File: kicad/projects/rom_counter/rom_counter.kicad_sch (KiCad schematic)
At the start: 42 parts, among them J1 peripheral_addr_bus_connector, J2 peripheral_aux_connector, J3 peripheral_membank_connector, J4 Conn_02x16_Odd_Even, J5 Conn_01x16_Socket, J6 Conn_01x02_Socket, J7 Conn_01x02_Pin, U1 28C256, U10 74HC161, U11 74HC245, U12 74HC245, U2 28C256, U3 74HC30, U4 74HC30, U5 74HC32, U6 74HC00, U7 74HC161, U8 74HC161, U9 74HC161

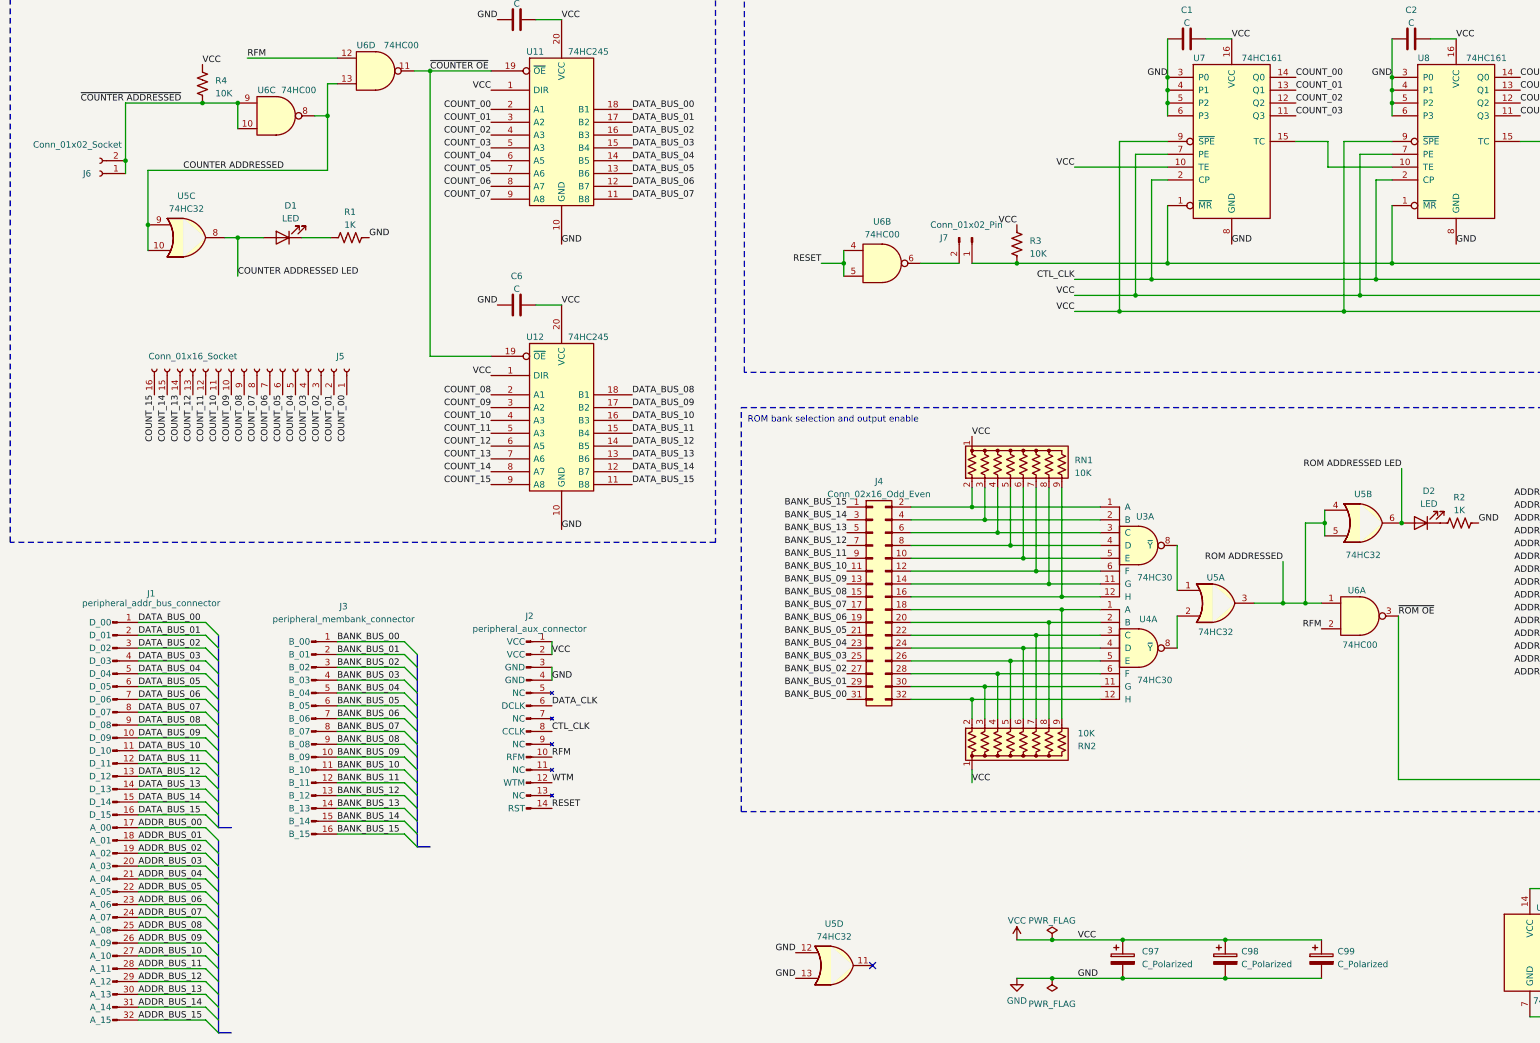
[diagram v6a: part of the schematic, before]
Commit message: PCB for ROM counter done - still needs tech checks
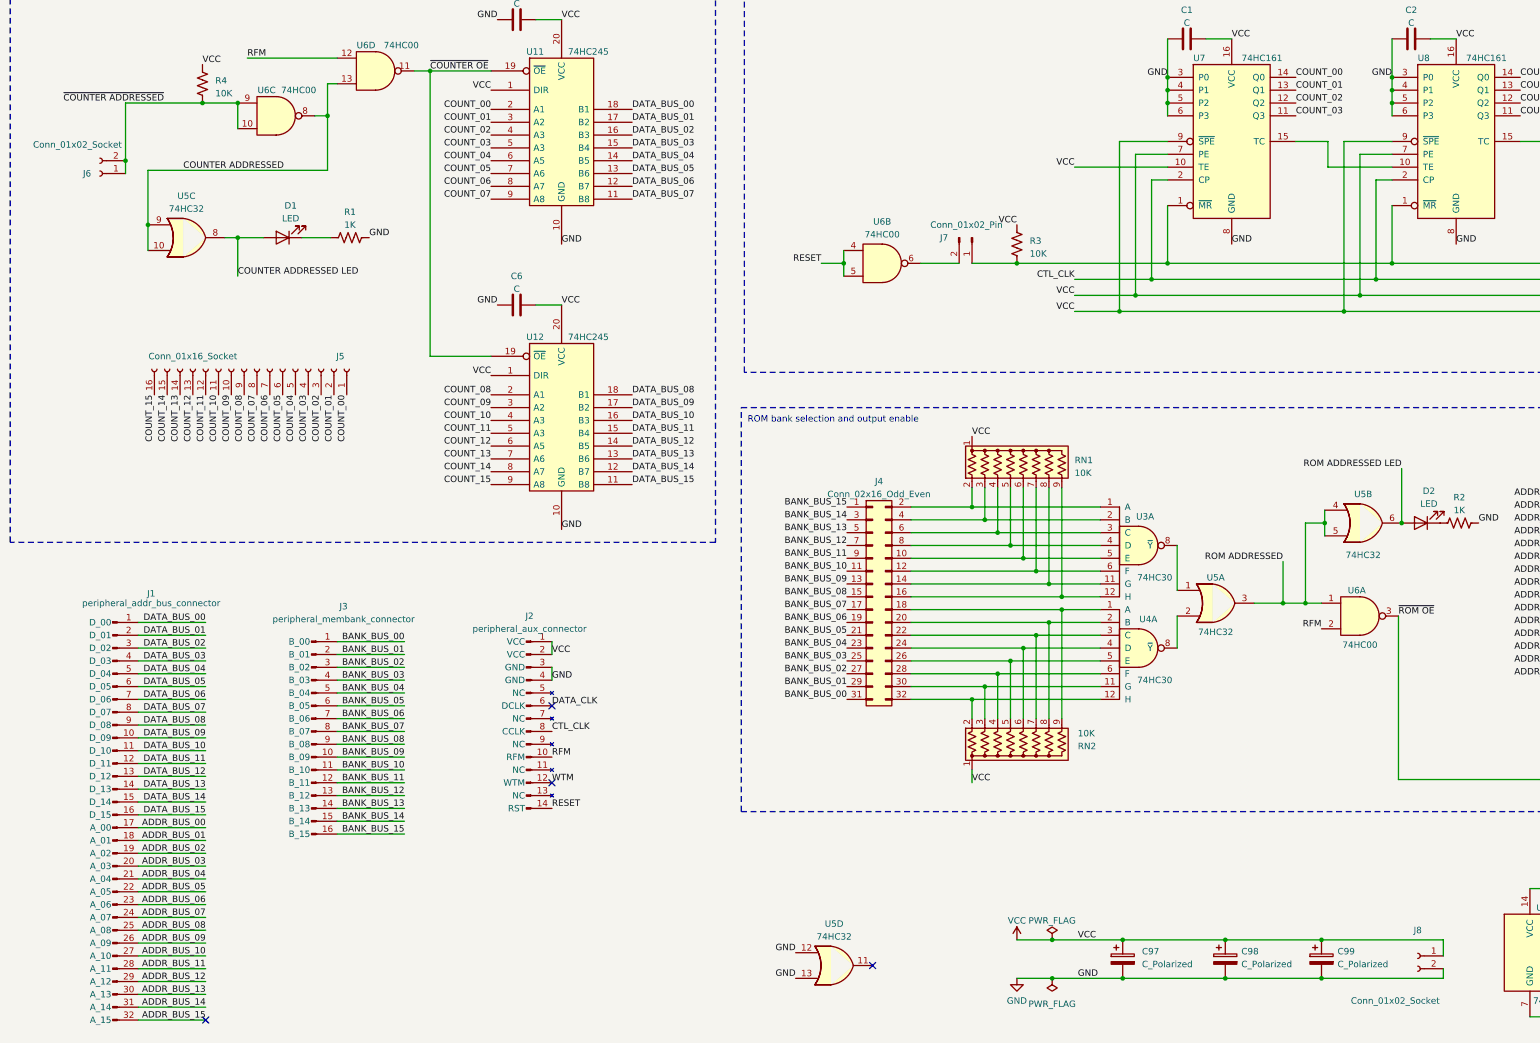
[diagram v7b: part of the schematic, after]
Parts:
- added J8: Conn_01x02_Socket, Connector_PinSocket_2.54mm:PinSocket_1x02_P2.54mm_Horizontal, symbol Connector:Conn_01x02_Socket
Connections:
- net GND: now also J8.2 (Pin_2)
- net VCC: now also J8.1 (Pin_1)
- net ~{COUNTER ADDRESSED}: now also J6.1 (Pin_1), J6.2 (Pin_2), R4.1, U6.10, U6.9
- no-connect marks 2 -> 5

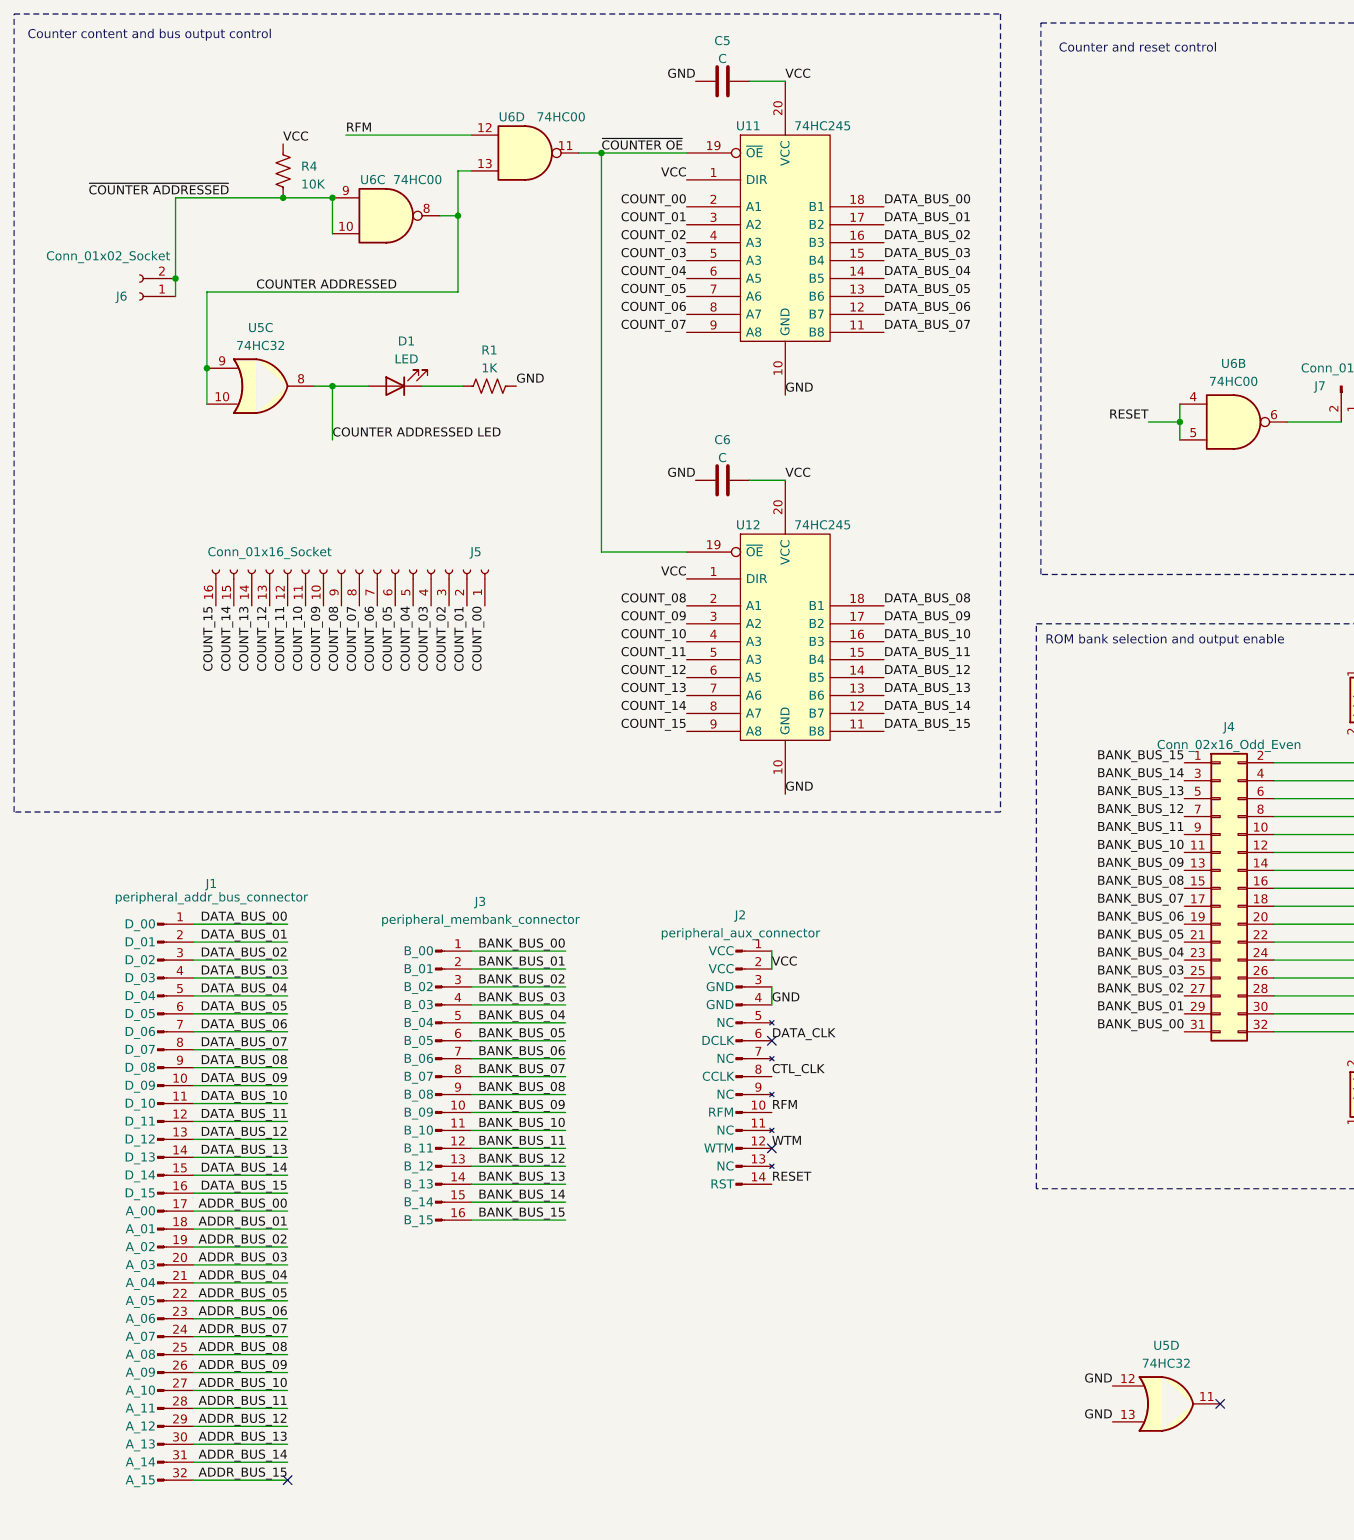
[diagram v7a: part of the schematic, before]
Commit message: Un invert counter addressed. Almost done on peripheral connect PCB.
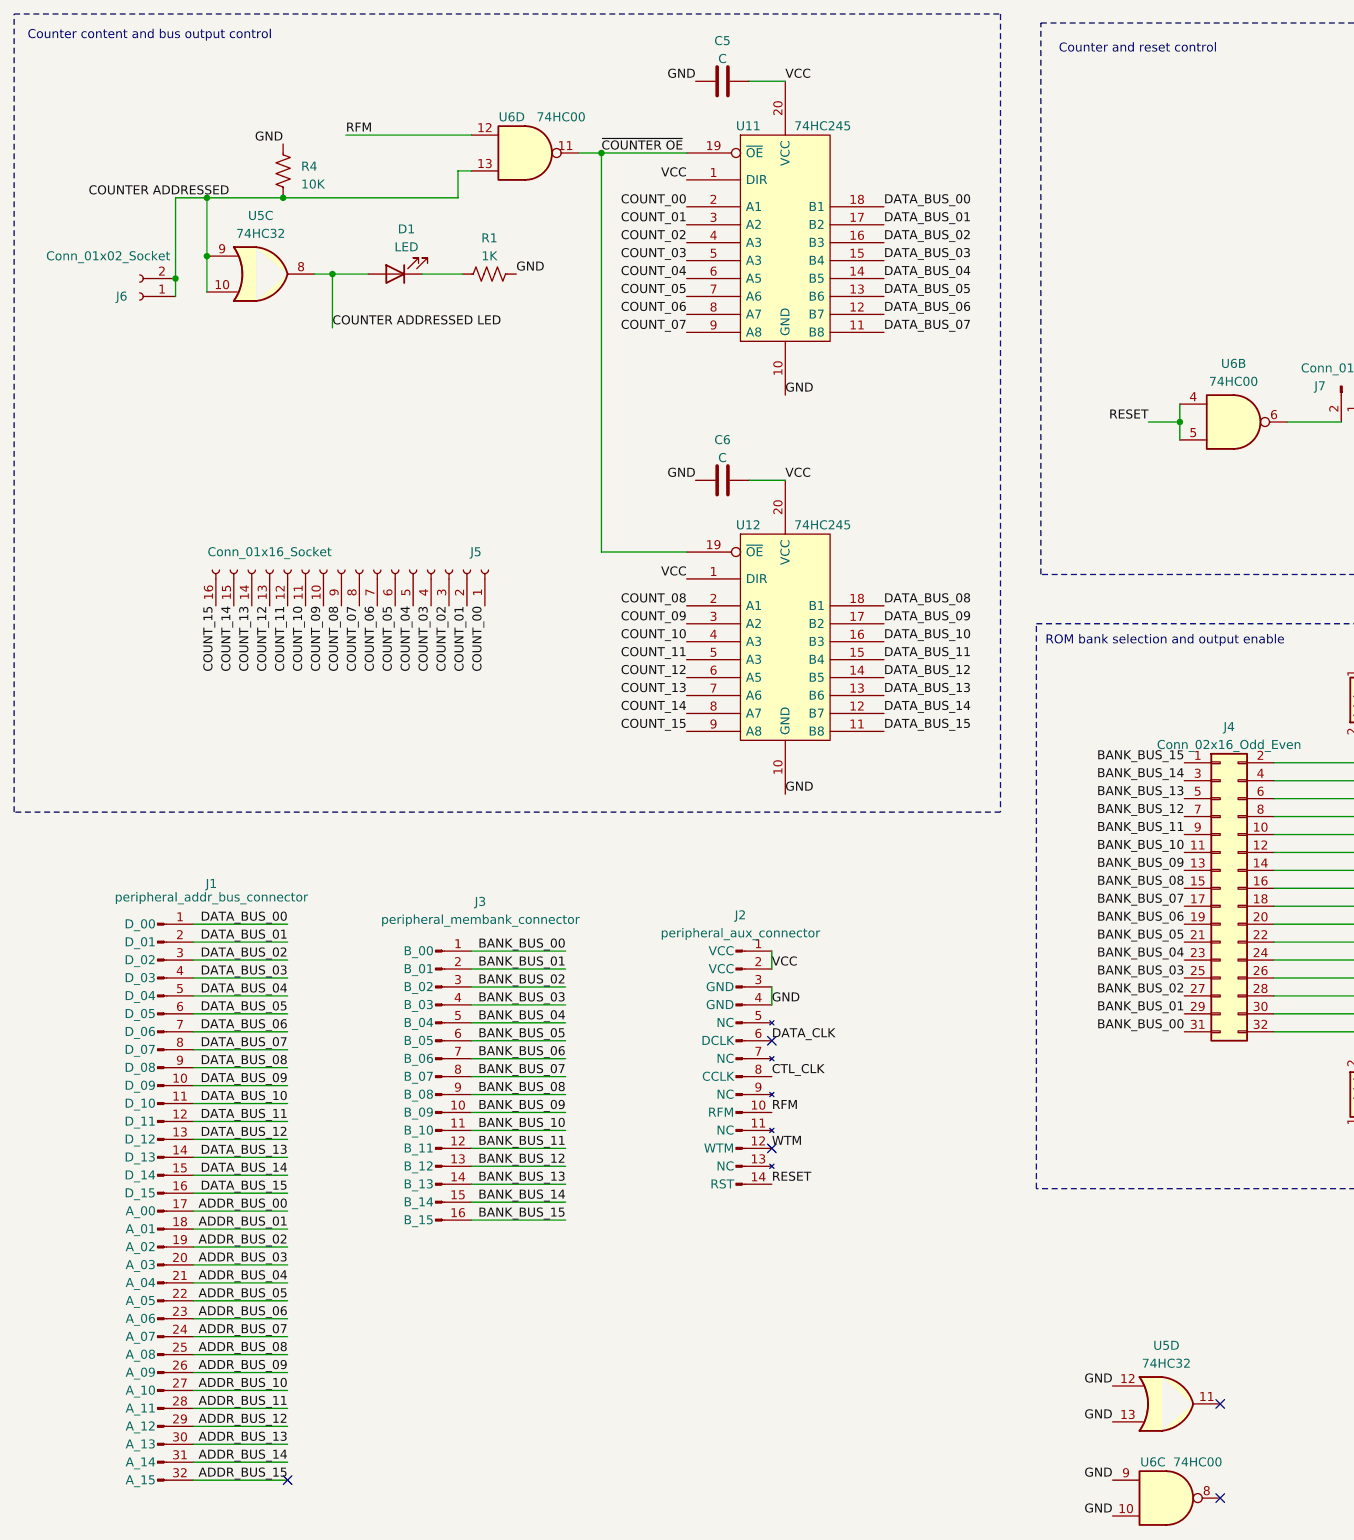
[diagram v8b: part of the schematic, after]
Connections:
- net COUNTER ADDRESSED: now also J6.1 (Pin_1), J6.2 (Pin_2), R4.1; no longer U6.8
- net GND: now also R4.2, U6.10, U6.9
- net VCC: no longer R4.2
- removed net ~{COUNTER ADDRESSED}: J6.1 (Pin_1), J6.2 (Pin_2), R4.1, U6.10, U6.9
- no-connect marks 5 -> 6
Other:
- moved on the sheet: D1, R1, U5C, U6C
